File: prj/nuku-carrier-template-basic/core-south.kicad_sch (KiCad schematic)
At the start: 19 parts, among them J1 DF40HC(4.0)-90DS-0.4V, SW1 PROG

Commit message: Route template.basic
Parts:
- R12: value 330 -> 1k; LCSC C25104 -> C11702
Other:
- moved on the sheet: R10, R11, R3, R4, R5, R6, R7, R8, R9

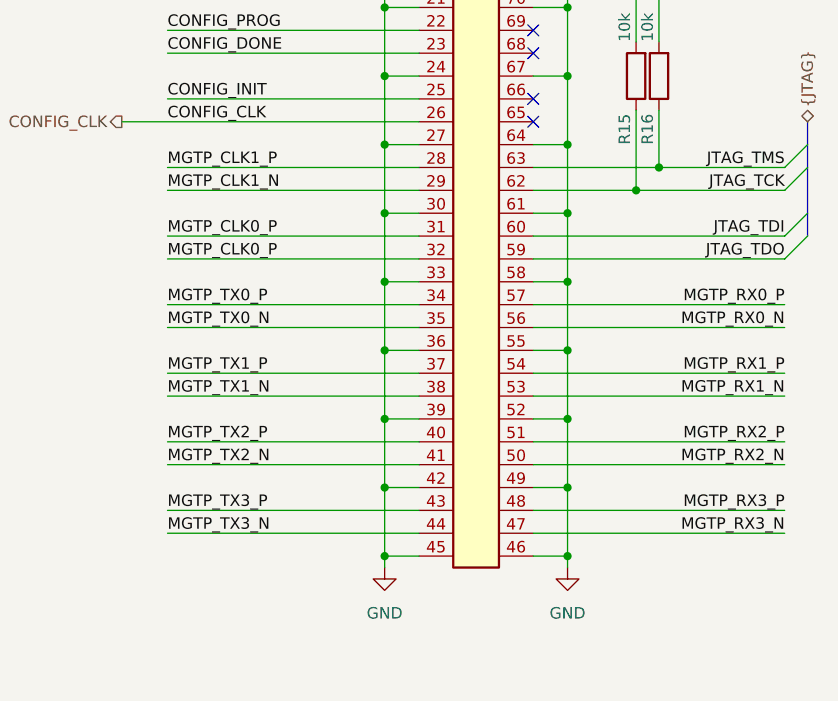
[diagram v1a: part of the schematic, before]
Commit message: Finish template.basic + Production outputs
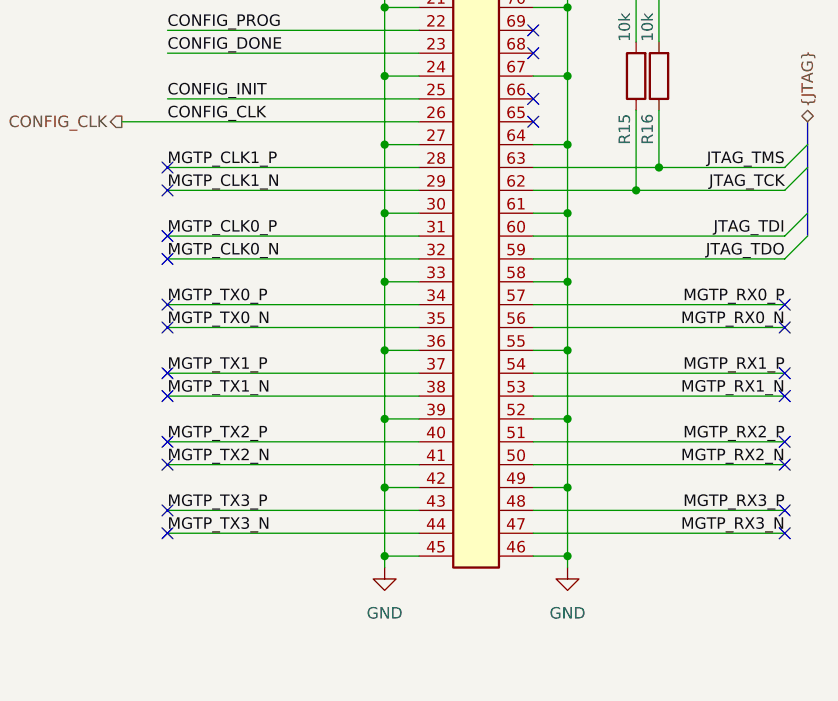
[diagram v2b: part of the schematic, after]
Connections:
- net MGTP_CLK0_P: no longer J1.32
- new net MGTP_CLK0_N: J1.32
- no-connect marks 10 -> 30
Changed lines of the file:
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@@
+	)
+	(no_connect
+		(at 191.77 124.46)
+	)
+	(no_connect
+		(at 260.35 142.24)
 	)
 	(no_connect
@@
 	)
 	(no_connect
+		(at 191.77 134.62)
+	)
+	(no_connect
+		(at 191.77 111.76)
+	)
+	(no_connect
 		(at 232.41 73.66)
 	)
@@
 	)
 	(no_connect
+		(at 191.77 132.08)
+	)
+	(no_connect
+		(at 260.35 127)
+	)
+	(no_connect
 		(at 232.41 93.98)
 	)
 	(no_connect
+		(at 260.35 139.7)
+	)
+	(no_connect
 		(at 232.41 101.6)
 	)
 	(no_connect
+		(at 260.35 132.08)
+	)
+	(no_connect
+		(at 191.77 147.32)
+	)
+	(no_connect
+		(at 260.35 149.86)
+	)
+	(no_connect
+		(at 191.77 149.86)
+	)
+	(no_connect
+		(at 191.77 127)
+	)
+	(no_connect
 		(at 232.41 104.14)
 	)
 	(no_connect
+		(at 191.77 142.24)
+	)
+	(no_connect
+		(at 191.77 139.7)
+	)
+	(no_connect
+		(at 191.77 109.22)
+	)
+	(no_connect
 		(at 232.41 96.52)
 	)
 	(no_connect
+		(at 260.35 124.46)
+	)
+	(no_connect
+		(at 191.77 116.84)
+	)
+	(no_connect
 		(at 232.41 78.74)
 	)
 	(no_connect
+		(at 260.35 147.32)
+	)
+	(no_connect
 		(at 232.41 88.9)
+	)
+	(no_connect
+		(at 191.77 119.38)
+	)
+	(no_connect
+		(at 260.35 134.62)
 	)
 	(no_connect
@@
 		)
 	)
-	(label "MGTP_CLK0_P"
+	(label "MGTP_CLK0_N"
 		(at 191.77 119.38 0)
 		(effects
